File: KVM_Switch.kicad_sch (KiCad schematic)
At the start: 0 parts

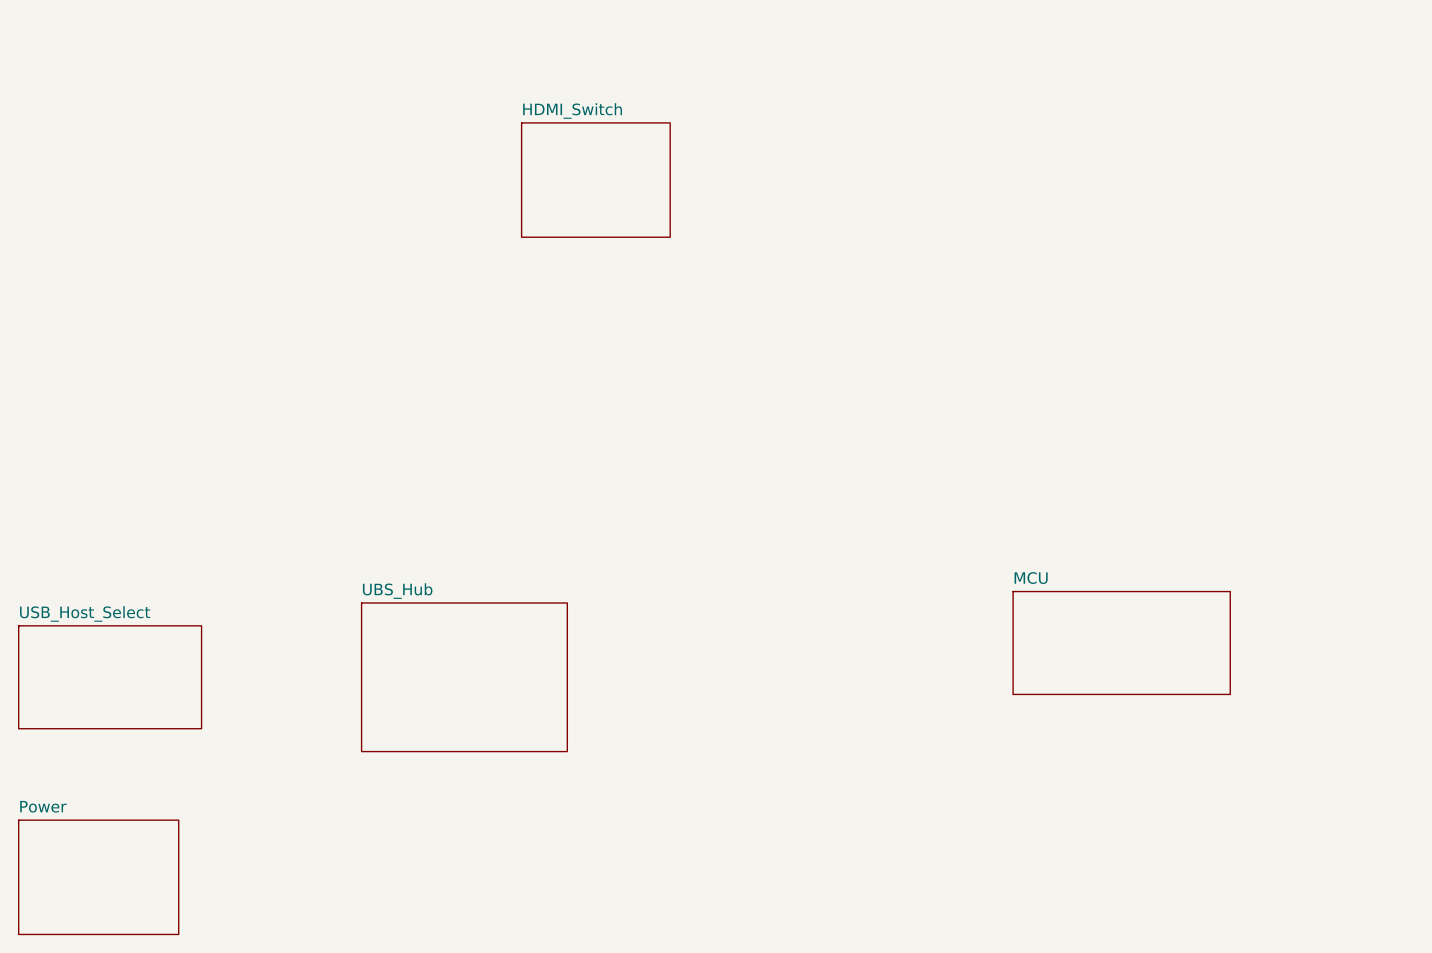
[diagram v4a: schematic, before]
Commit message: Changed MCU & Stared routing HDMI connectiors
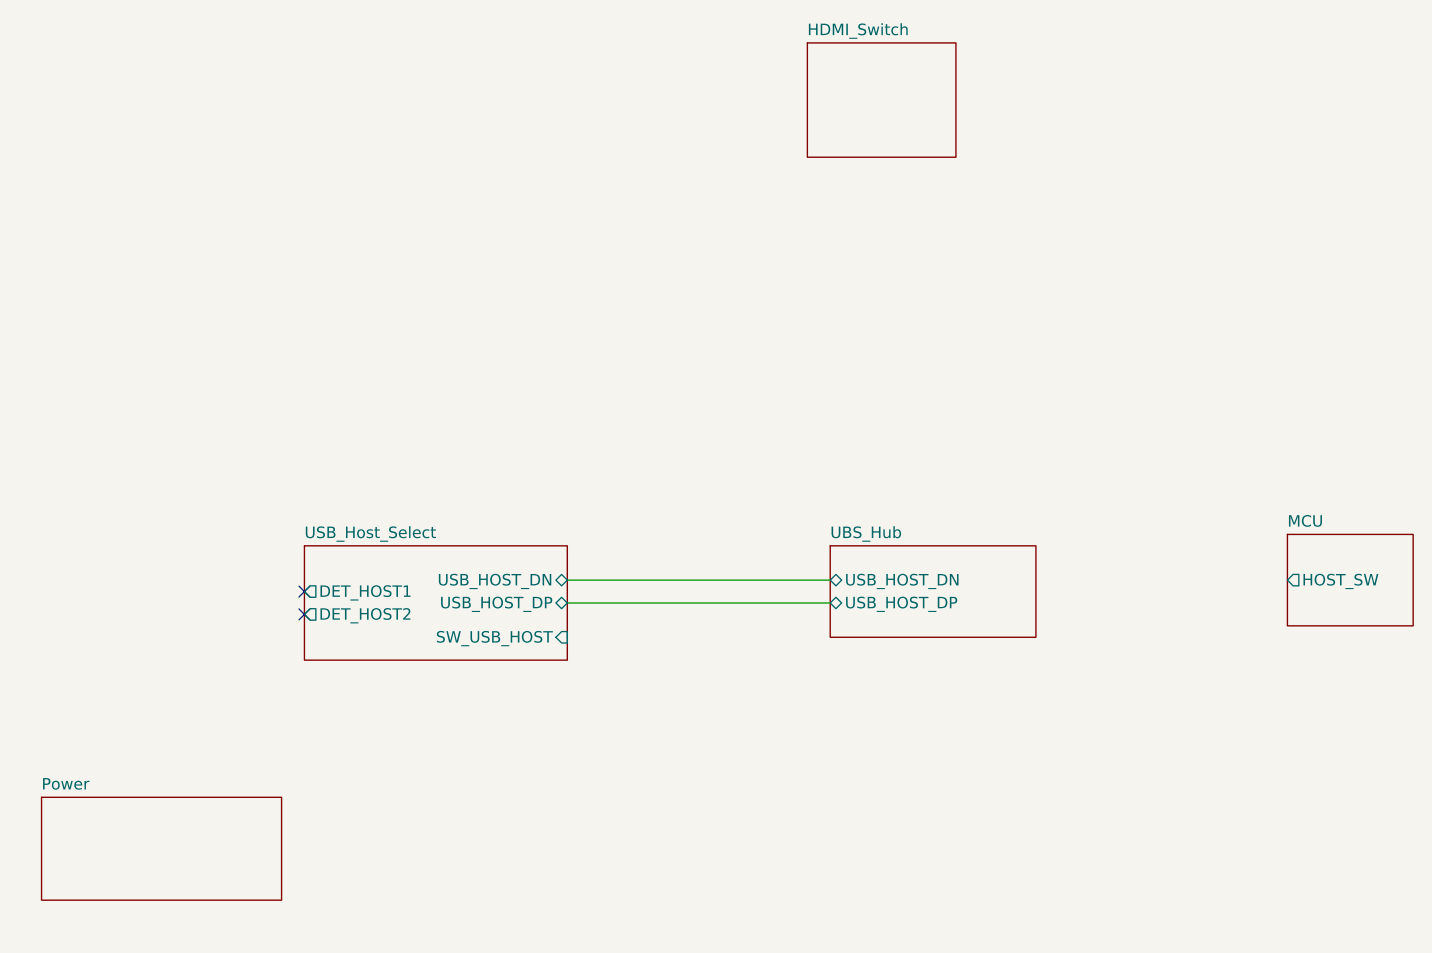
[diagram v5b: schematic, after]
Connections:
- no-connect marks 0 -> 2
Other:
- sheet MCU ports: added HOST_SW; removed none
- sheet UBS_Hub ports: added USB_HOST_DN, USB_HOST_DP; removed none
- sheet USB_Host_Select ports: added DET_HOST1, DET_HOST2, SW_USB_HOST, USB_HOST_DN, USB_HOST_DP; removed none
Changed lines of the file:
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@@
 		(rev "A")
 	)
-	(sheet
-		(at 97.79 105.41)
-		(size 22.86 16.51)
+	(no_connect
+		(at 91.44 106.68)
+	)
+	(no_connect
+		(at 91.44 104.14)
+	)
+	(wire
+		(pts
+			(xy 120.65 105.41) (xy 149.86 105.41)
+		)
+		(stroke
+			(width 0)
+			(type default)
+		)
+	)
+	(wire
+		(pts
+			(xy 120.65 102.87) (xy 149.86 102.87)
+		)
+		(stroke
+			(width 0)
+			(type default)
+		)
+	)
+	(sheet
+		(at 149.86 99.06)
+		(size 22.86 10.16)
 		(exclude_from_sim no)
 		(in_bom yes)
@@
 		)
 		(property "Sheetname" "UBS_Hub"
-			(at 97.79 104.6984 0)
+			(at 149.86 98.3484 0)
 			(show_name no)
 			(do_not_autoplace no)
@@
 		)
 		(property "Sheetfile" "USB_Hub.kicad_sch"
-			(at 97.79 122.5046 0)
-			(hide yes)
-			(show_name no)
-			(do_not_autoplace no)
-			(effects
-				(font
-					(size 1.27 1.27)
-				)
-				(justify left top)
+			(at 149.86 109.8046 0)
+			(hide yes)
+			(show_name no)
+			(do_not_autoplace no)
+			(effects
+				(font
+					(size 1.27 1.27)
+				)
+				(justify left top)
+			)
+		)
+		(pin "USB_HOST_DN" bidirectional
+			(at 149.86 102.87 180)
+			(effects
+				(font
+					(size 1.27 1.27)
+				)
+				(justify left)
+			)
+		)
+		(pin "USB_HOST_DP" bidirectional
+			(at 149.86 105.41 180)
+			(effects
+				(font
+					(size 1.27 1.27)
+				)
+				(justify left)
 			)
 		)
@@
 	)
 	(sheet
-		(at 59.69 129.54)
-		(size 17.78 12.7)
+		(at 62.23 127)
+		(size 26.67 11.43)
 		(exclude_from_sim no)
 		(in_bom yes)
@@
 		)
 		(property "Sheetname" "Power"
-			(at 59.69 128.8284 0)
+			(at 62.23 126.2884 0)
 			(show_name no)
 			(do_not_autoplace no)
@@
 		)
 		(property "Sheetfile" "Power.kicad_sch"
-			(at 59.69 142.8246 0)
+			(at 62.23 139.0146 0)
 			(hide yes)
 			(show_name no)
@@
 	)
 	(sheet
-		(at 115.57 52.07)
+		(at 147.32 43.18)
 		(size 16.51 12.7)
 		(exclude_from_sim no)
@@
 		)
 		(property "Sheetname" "HDMI_Switch"
-			(at 115.57 51.3584 0)
+			(at 147.32 42.4684 0)
 			(show_name no)
 			(do_not_autoplace no)
@@
 		)
 		(property "Sheetfile" "HDMI_Switch.kicad_sch"
-			(at 115.57 65.3546 0)
+			(at 147.32 56.4646 0)
 			(hide yes)
 			(show_name no)
@@
 	)
 	(sheet
-		(at 59.69 107.95)
-		(size 20.32 11.43)
+		(at 91.44 99.06)
+		(size 29.21 12.7)
 		(exclude_from_sim no)
 		(in_bom yes)
@@
 		)
 		(property "Sheetname" "USB_Host_Select"
-			(at 59.69 107.2384 0)
+			(at 91.44 98.3484 0)
 			(show_name no)
 			(do_not_autoplace no)
@@
 		)
 		(property "Sheetfile" "USB_Host_Select.kicad_sch"
-			(at 59.69 119.9646 0)
-			(hide yes)
-			(show_name no)
-			(do_not_autoplace no)
-			(effects
-				(font
-					(size 1.27 1.27)
-				)
-				(justify left top)
+			(at 91.44 112.3446 0)
+			(hide yes)
+			(show_name no)
+			(do_not_autoplace no)
+			(effects
+				(font
+					(size 1.27 1.27)
+				)
+				(justify left top)
+			)
+		)
+		(pin "DET_HOST1" output
+			(at 91.44 104.14 180)
+			(effects
+				(font
+					(size 1.27 1.27)
+				)
+				(justify left)
+			)
+		)
+		(pin "DET_HOST2" output
+			(at 91.44 106.68 180)
+			(effects
+				(font
+					(size 1.27 1.27)
+				)
+				(justify left)
+			)
+		)
+		(pin "SW_USB_HOST" input
+			(at 120.65 109.22 0)
+			(effects
+				(font
+					(size 1.27 1.27)
+				)
+				(justify right)
+			)
+		)
+		(pin "USB_HOST_DN" bidirectional
+			(at 120.65 102.87 0)
+			(effects
+				(font
+					(size 1.27 1.27)
+				)
+				(justify right)
+			)
+		)
+		(pin "USB_HOST_DP" bidirectional
+			(at 120.65 105.41 0)
+			(effects
+				(font
+					(size 1.27 1.27)
+				)
+				(justify right)
 			)
 		)
@@
 	)
 	(sheet
-		(at 170.18 104.14)
-		(size 24.13 11.43)
+		(at 200.66 97.79)
+		(size 13.97 10.16)
 		(exclude_from_sim no)
 		(in_bom yes)
@@
 		)
 		(property "Sheetname" "MCU"
-			(at 170.18 103.4284 0)
+			(at 200.66 97.0784 0)
 			(show_name no)
 			(do_not_autoplace no)
@@
 		)
 		(property "Sheetfile" "MCU.kicad_sch"
-			(at 170.18 116.1546 0)
-			(hide yes)
-			(show_name no)
-			(do_not_autoplace no)
-			(effects
-				(font
-					(size 1.27 1.27)
-				)
-				(justify left top)
-			)
-		)
+			(at 200.66 108.5346 0)
+			(hide yes)
+			(show_name no)
+			(do_not_autoplace no)
+			(effects
+				(font
+					(size 1.27 1.27)
+				)
+				(justify left top)
+			)
+		)
+		(pin "HOST_SW" output
+			(at 200.66 102.87 180)
+			(effects
+				(font
+					(size 1.27 1.27)
+				)
+				(justify left)
+			)
+		)

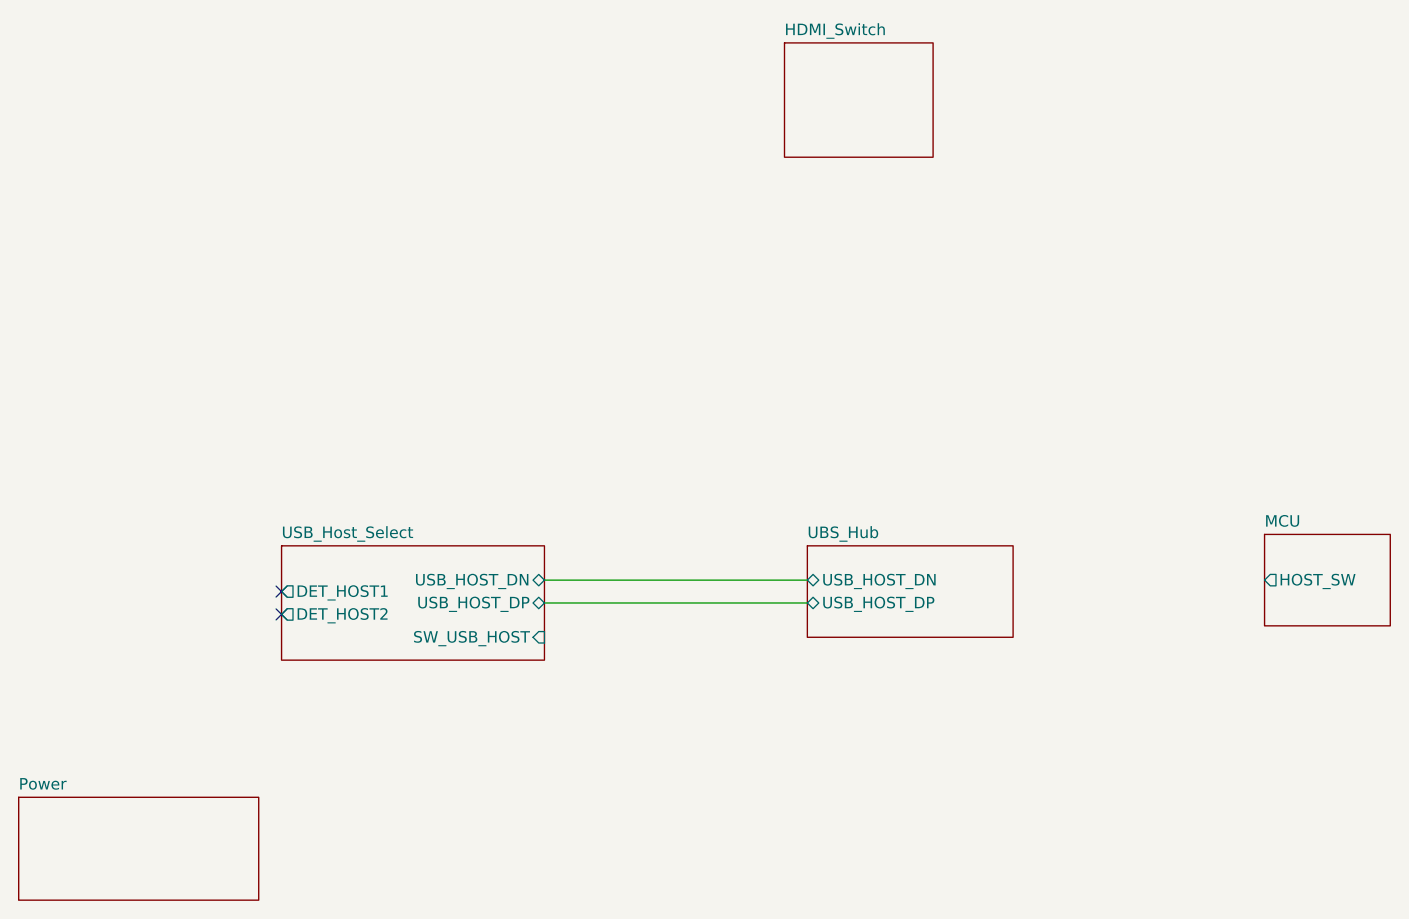
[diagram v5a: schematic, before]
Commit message: HDMI schematics
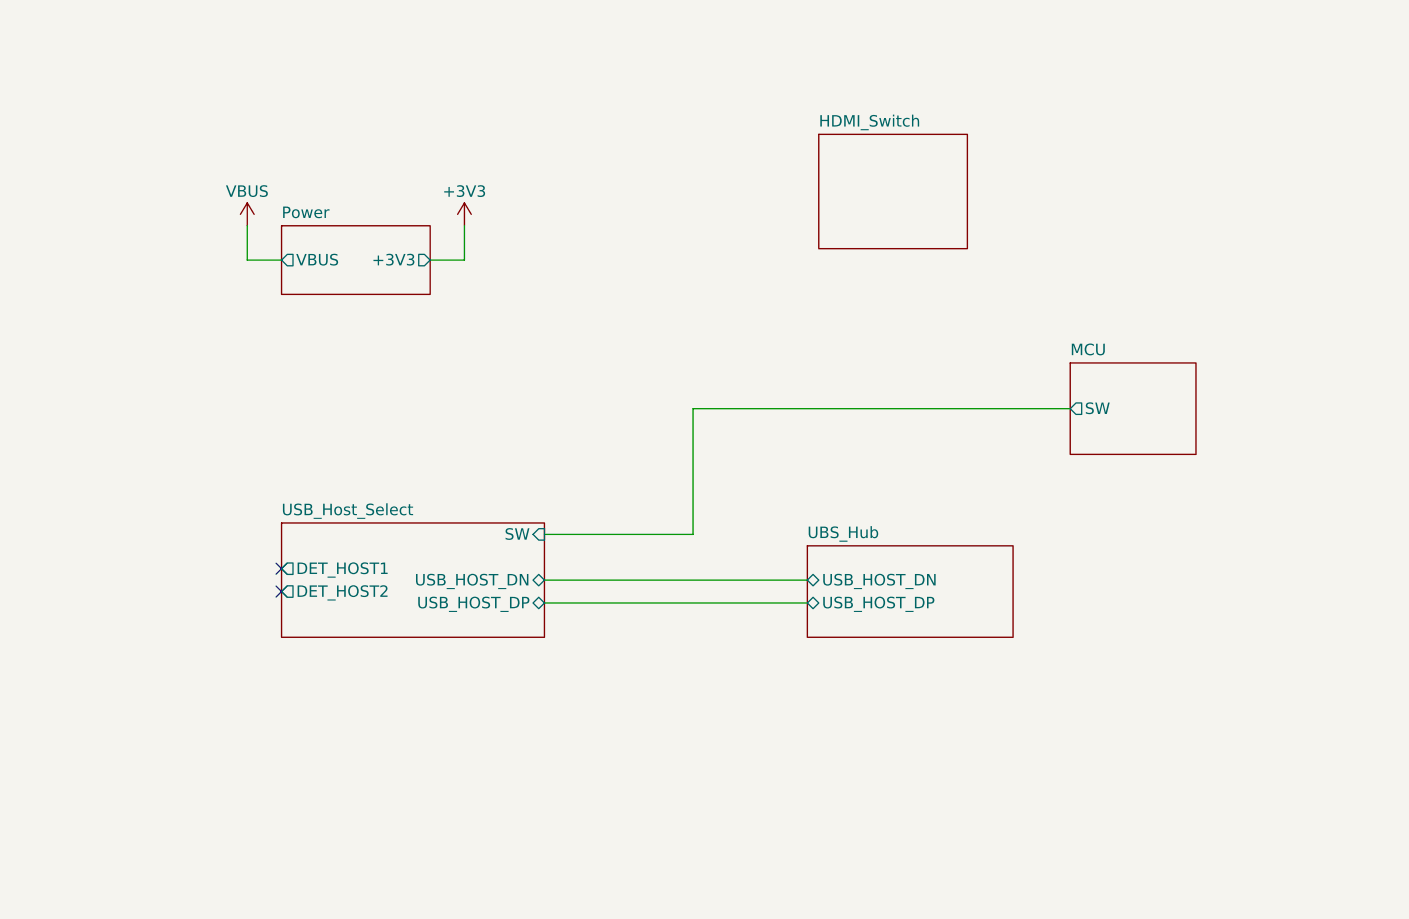
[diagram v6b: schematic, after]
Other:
- sheet MCU ports: added SW; removed HOST_SW
- sheet Power ports: added +3V3, VBUS; removed none
- sheet USB_Host_Select ports: added SW; removed SW_USB_HOST

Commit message: Schematics done
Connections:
- no-connect marks 2 -> 0
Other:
- sheet HDMI_Switch ports: added DET_A, DET_B, SW; removed none
- sheet MCU ports: added DET_A, DET_B, UP_DET; removed none
- sheet UBS_Hub ports: added UP_DET, USB_UP_DN, USB_UP_DP; removed USB_HOST_DN, USB_HOST_DP
- sheet USB_Host_Select ports: added USB_UP_DN, USB_UP_DP; removed DET_HOST1, DET_HOST2, USB_HOST_DN, USB_HOST_DP
